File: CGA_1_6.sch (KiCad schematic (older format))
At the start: 19 parts, among them U13 74LS08, U14 74LS32, U28 74LS10, U38 MC6845, U48 74LS51, U49 74LS02, U50 2118, U51 2118, U52 2118, U53 2118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

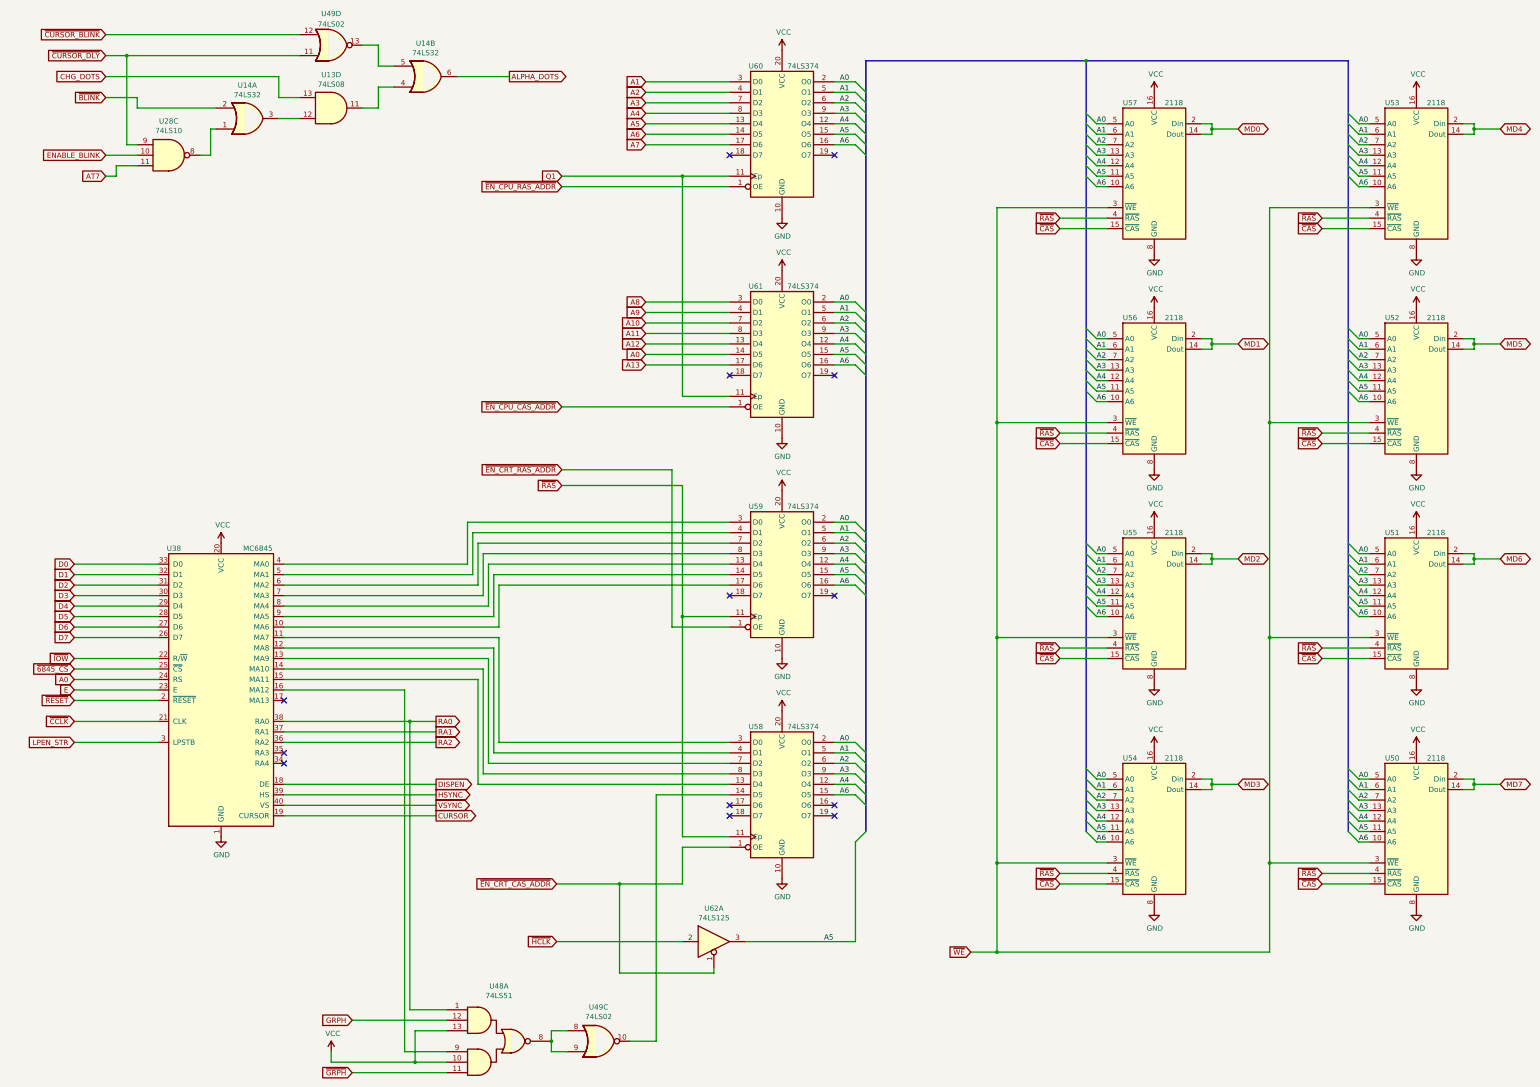
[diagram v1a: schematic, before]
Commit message: Fix RAM bus connections
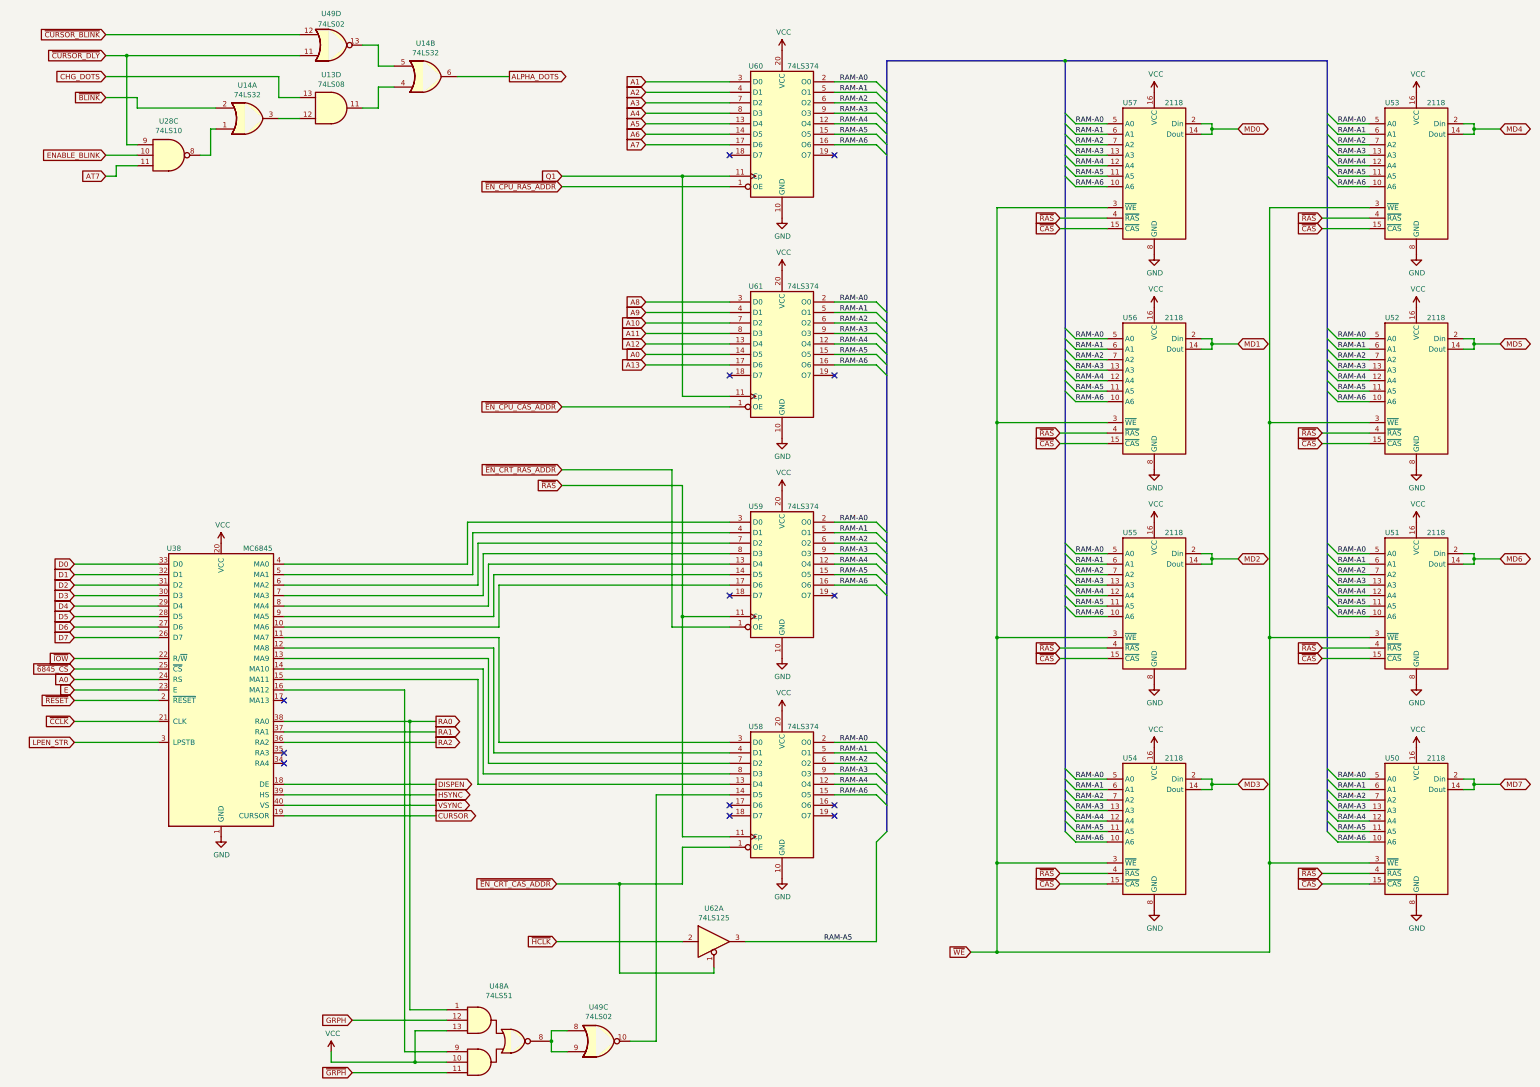
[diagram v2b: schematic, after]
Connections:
- net A0: no longer U50.5 (A0), U51.5 (A0), U52.5 (A0), U53.5 (A0), U54.5 (A0), U55.5 (A0), U56.5 (A0), U57.5 (A0), U58.2 (O0), U59.2 (O0), U60.2 (O0), U61.2 (O0)
- net A1: no longer U50.6 (A1), U51.6 (A1), U52.6 (A1), U53.6 (A1), U54.6 (A1), U55.6 (A1), U56.6 (A1), U57.6 (A1), U58.5 (O1), U59.5 (O1), U60.5 (O1), U61.5 (O1)
- net A2: no longer U50.7 (A2), U51.7 (A2), U52.7 (A2), U53.7 (A2), U54.7 (A2), U55.7 (A2), U56.7 (A2), U57.7 (A2), U58.6 (O2), U59.6 (O2), U60.6 (O2), U61.6 (O2)
- net A3: no longer U50.13 (A3), U51.13 (A3), U52.13 (A3), U53.13 (A3), U54.13 (A3), U55.13 (A3), U56.13 (A3), U57.13 (A3), U58.9 (O3), U59.9 (O3), U60.9 (O3), U61.9 (O3)
- net A4: no longer U50.12 (A4), U51.12 (A4), U52.12 (A4), U53.12 (A4), U54.12 (A4), U55.12 (A4), U56.12 (A4), U57.12 (A4), U58.12 (O4), U59.12 (O4), U60.12 (O4), U61.12 (O4)
- net A5: no longer U50.11 (A5), U51.11 (A5), U52.11 (A5), U53.11 (A5), U54.11 (A5), U55.11 (A5), U56.11 (A5), U57.11 (A5), U59.15 (O5), U60.15 (O5), U61.15 (O5), U62.3
- net A6: no longer U50.10 (A6), U51.10 (A6), U52.10 (A6), U53.10 (A6), U54.10 (A6), U55.10 (A6), U56.10 (A6), U57.10 (A6), U58.15 (O5), U59.16 (O6), U60.16 (O6), U61.16 (O6)
- new net RAM-A0: U50.5 (A0), U51.5 (A0), U52.5 (A0), U53.5 (A0), U54.5 (A0), U55.5 (A0), U56.5 (A0), U57.5 (A0), U58.2 (O0), U59.2 (O0), U60.2 (O0), U61.2 (O0)
- new net RAM-A1: U50.6 (A1), U51.6 (A1), U52.6 (A1), U53.6 (A1), U54.6 (A1), U55.6 (A1), U56.6 (A1), U57.6 (A1), U58.5 (O1), U59.5 (O1), U60.5 (O1), U61.5 (O1)
- new net RAM-A2: U50.7 (A2), U51.7 (A2), U52.7 (A2), U53.7 (A2), U54.7 (A2), U55.7 (A2), U56.7 (A2), U57.7 (A2), U58.6 (O2), U59.6 (O2), U60.6 (O2), U61.6 (O2)
- new net RAM-A3: U50.13 (A3), U51.13 (A3), U52.13 (A3), U53.13 (A3), U54.13 (A3), U55.13 (A3), U56.13 (A3), U57.13 (A3), U58.9 (O3), U59.9 (O3), U60.9 (O3), U61.9 (O3)
- new net RAM-A4: U50.12 (A4), U51.12 (A4), U52.12 (A4), U53.12 (A4), U54.12 (A4), U55.12 (A4), U56.12 (A4), U57.12 (A4), U58.12 (O4), U59.12 (O4), U60.12 (O4), U61.12 (O4)
- new net RAM-A5: U50.11 (A5), U51.11 (A5), U52.11 (A5), U53.11 (A5), U54.11 (A5), U55.11 (A5), U56.11 (A5), U57.11 (A5), U59.15 (O5), U60.15 (O5), U61.15 (O5), U62.3
- new net RAM-A6: U50.10 (A6), U51.10 (A6), U52.10 (A6), U53.10 (A6), U54.10 (A6), U55.10 (A6), U56.10 (A6), U57.10 (A6), U58.15 (O5), U59.16 (O6), U60.16 (O6), U61.16 (O6)

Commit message: Fix some more flags and footprints
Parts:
- U62: footprint Package_DIP:DIP-14_W10.16mm_LongPads -> Package_DIP:DIP-14_W7.62mm_LongPads
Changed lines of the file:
@@
 U 1 1 60464055
 P 12350 2700
+AR Path="/60464055" Ref="U57"  Part="1"
+AR Path="/60463BAE/60464055" Ref="U57"  Part="1"
 F 0 "U57" H 11900 3800 50  0000 L CNN
 F 1 "2118" H 12300 3800 50  0000 L CNN
@@
 U 1 1 60467794
 P 12350 4750
+AR Path="/60467794" Ref="U56"  Part="1"
+AR Path="/60463BAE/60467794" Ref="U56"  Part="1"
 F 0 "U56" H 11900 5850 50  0000 L CNN
 F 1 "2118" H 12300 5850 50  0000 L CNN
@@
 U 1 1 60469A6E
 P 12350 6800
+AR Path="/60469A6E" Ref="U55"  Part="1"
+AR Path="/60463BAE/60469A6E" Ref="U55"  Part="1"
 F 0 "U55" H 11900 7900 50  0000 L CNN
 F 1 "2118" H 12300 7900 50  0000 L CNN
@@
 Wire Wire Line
 	12750 6000 12650 6000
-$Comp
-L power:GND #PWR0111
-U 1 1 60472FFD
-P 12200 9300
-F 0 "#PWR0111" H 12200 9050 50  0001 C CNN
-F 1 "GND" H 12205 9127 50  0000 C CNN
-F 2 "" H 12200 9300 50  0001 C CNN
-F 3 "" H 12200 9300 50  0001 C CNN
-	1    12200 9300
-	1    0    0    -1
-$EndComp
 $Comp
 L power:VCC #PWR0112
@@
 U 1 1 604730D9
 P 12350 8950
+AR Path="/604730D9" Ref="U54"  Part="1"
+AR Path="/60463BAE/604730D9" Ref="U54"  Part="1"
 F 0 "U54" H 11900 10050 50  0000 L CNN
 F 1 "2118" H 12300 10050 50  0000 L CNN
@@
 U 1 1 6047C58C
 P 14850 2700
+AR Path="/6047C58C" Ref="U53"  Part="1"
+AR Path="/60463BAE/6047C58C" Ref="U53"  Part="1"
 F 0 "U53" H 14400 3800 50  0000 L CNN
 F 1 "2118" H 14800 3800 50  0000 L CNN
@@
 U 1 1 6047C5AD
 P 14850 4750
+AR Path="/6047C5AD" Ref="U52"  Part="1"
+AR Path="/60463BAE/6047C5AD" Ref="U52"  Part="1"
 F 0 "U52" H 14400 5850 50  0000 L CNN
 F 1 "2118" H 14800 5850 50  0000 L CNN
@@
 U 1 1 6047C5CE
 P 14850 6800
+AR Path="/6047C5CE" Ref="U51"  Part="1"
+AR Path="/60463BAE/6047C5CE" Ref="U51"  Part="1"
 F 0 "U51" H 14400 7900 50  0000 L CNN
 F 1 "2118" H 14800 7900 50  0000 L CNN
@@
 U 1 1 6047C5EF
 P 14850 8950
+AR Path="/6047C5EF" Ref="U50"  Part="1"
+AR Path="/60463BAE/6047C5EF" Ref="U50"  Part="1"
 F 0 "U50" H 14400 10050 50  0000 L CNN
 F 1 "2118" H 14800 10050 50  0000 L CNN
@@
 F 0 "U62" H 8000 9917 50  0000 C CNN
 F 1 "74LS125" H 8000 9826 50  0000 C CNN
-F 2 "Package_DIP:DIP-14_W10.16mm_LongPads" H 8000 9600 50  0001 C CNN
+F 2 "Package_DIP:DIP-14_W7.62mm_LongPads" H 8000 9600 50  0001 C CNN
 F 3 "http://www.ti.com/lit/gpn/sn74LS125" H 8000 9600 50  0001 C CNN
 	1    8000 9600
@@
 	13950 8650 14250 8650
 Wire Bus Line
+	13850 1200 13850 8550
+Wire Bus Line
 	9650 1200 9650 8550
 Wire Bus Line
 	11350 1200 11350 8550
-Wire Bus Line
-	13850 1200 13850 8550
+$Comp
+L power:GND #PWR0111
+U 1 1 60472FFD
+P 12200 9300
+F 0 "#PWR0111" H 12200 9050 50  0001 C CNN
+F 1 "GND" H 12205 9127 50  0000 C CNN
+F 2 "" H 12200 9300 50  0001 C CNN
+F 3 "" H 12200 9300 50  0001 C CNN
+	1    12200 9300
+	1    0    0    -1
+$EndComp
 $EndSCHEMATC
